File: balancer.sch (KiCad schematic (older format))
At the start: 11 parts, among them IC1 TLV3404, J1 S4B-XH-SM4-TB, J2 Output (+), J3 Output (-), J4 Input (+), J5 Input (-), Q1 IRF7455PBF

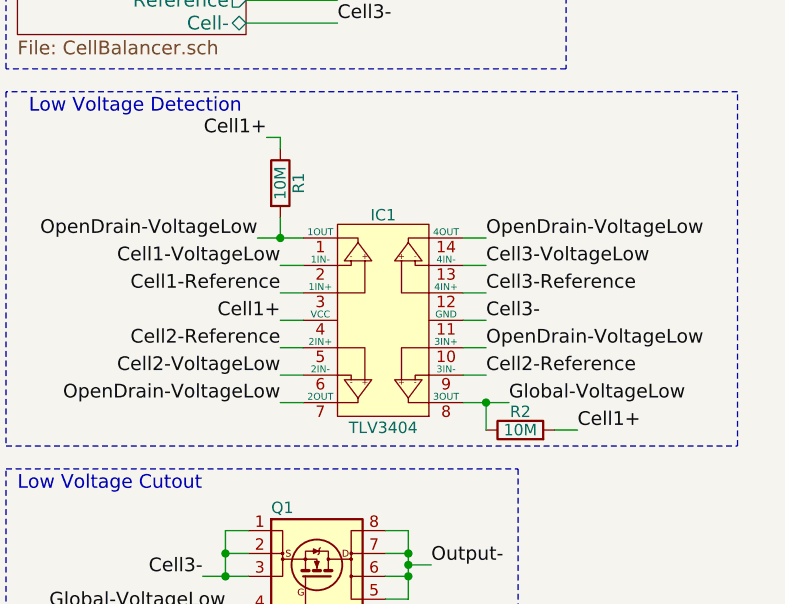
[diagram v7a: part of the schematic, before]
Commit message: changed the pull-ups on the TLV to 1M
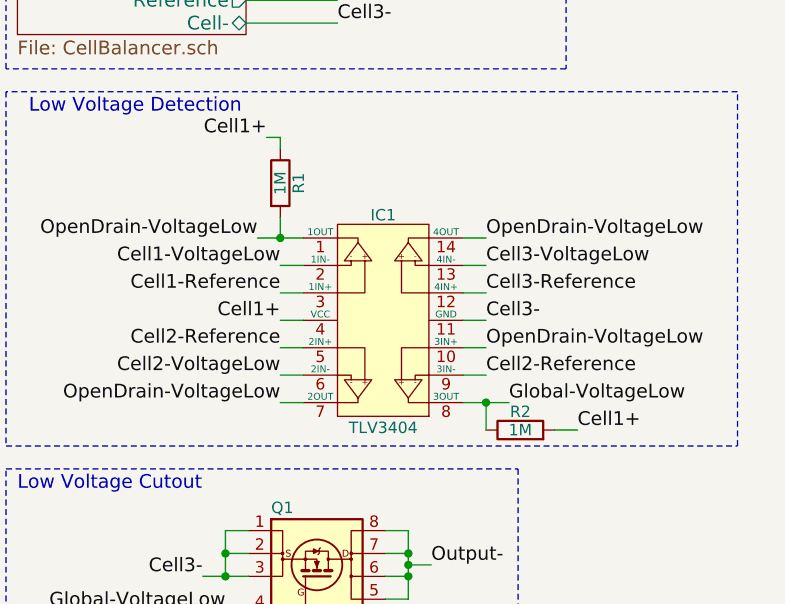
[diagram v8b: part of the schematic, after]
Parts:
- R1, R2: value 10M -> 1M
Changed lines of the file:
@@
 P 2120 4270
 F 0 "R1" V 2200 4270 50  0000 C CNN
-F 1 "10M" V 2120 4270 50  0000 C CNN
+F 1 "1M" V 2120 4270 50  0000 C CNN
 F 2 "Resistors_SMD:R_0805" V 2050 4270 50  0001 C CNN
 F 3 "" H 2120 4270 50  0001 C CNN
@@
 P 3170 5350
 F 0 "R2" V 3250 5350 50  0000 C CNN
-F 1 "10M" V 3170 5350 50  0000 C CNN
+F 1 "1M" V 3170 5350 50  0000 C CNN
 F 2 "Resistors_SMD:R_0805" V 3100 5350 50  0001 C CNN
 F 3 "" H 3170 5350 50  0001 C CNN
